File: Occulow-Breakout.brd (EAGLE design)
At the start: 100 x 80 mm, 21 parts, among them X1 SMA-SMD

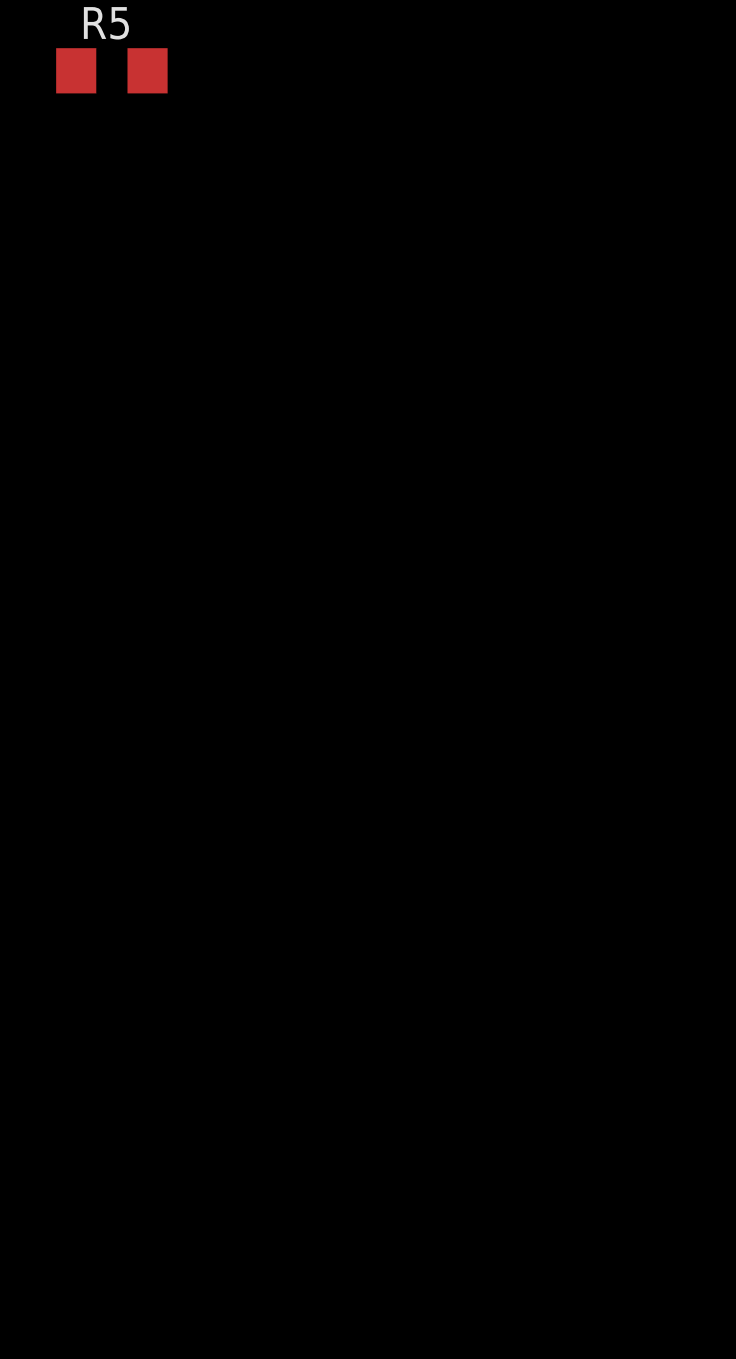
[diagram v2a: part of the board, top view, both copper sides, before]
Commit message: Separate vcc's, headers for all
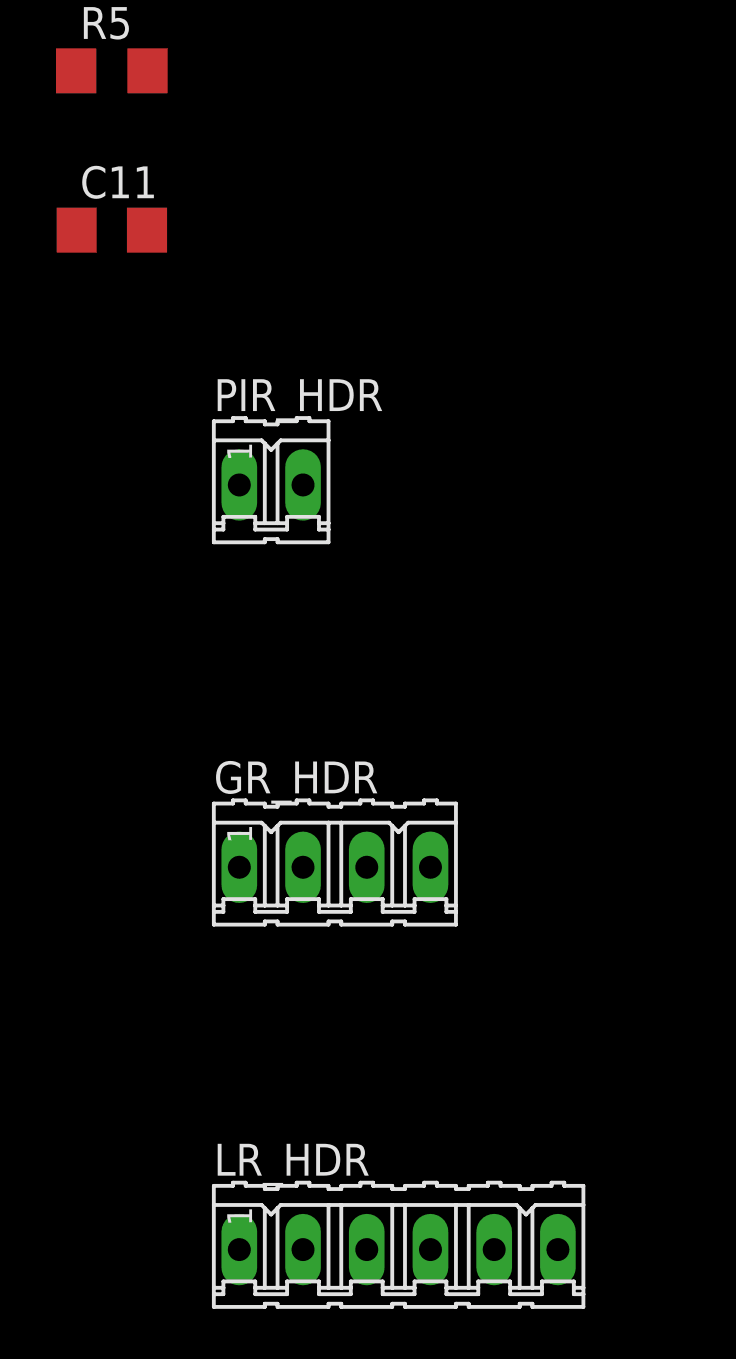
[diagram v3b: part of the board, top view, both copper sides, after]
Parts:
- added C11: 10uF, rcl:C1206
- added GR_HDR: (no value), con-amp-quick:04P
- added LR_HDR: (no value), con-amp-quick:06P
- added PIR_HDR: (no value), con-amp-quick:02P
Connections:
- removed net VCC: C1.1, R1.2, R2.2, R3.2, R5.2, U$2.13, U$2.9
- new net GR_VCC: C1.1, GR_HDR.4, R1.2, R2.2, R3.2, U$2.13, U$2.9
- new net LR_RST_N: LR_HDR.5, U$1.31
- new net LR_VCC: C11.1, LR_HDR.6, U$1.12, U$1.34
- new net PIR_VCC: PIR_HDR.2, R5.2
- net GND: now also C11.2
- net GR_INT: now also GR_HDR.1
- net GR_SCL: now also GR_HDR.2
- net GR_SDA: now also GR_HDR.3
- net LR_CTS: now also LR_HDR.2
- net LR_RTS: now also LR_HDR.1
- net LR_RX: now also LR_HDR.4
- net LR_TX: now also LR_HDR.3
- net PIR_OUT: now also PIR_HDR.1
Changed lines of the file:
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@@
 <element name="C10" library="rcl" package="C1206" value="100uF" x="-128.27" y="-71.12"/>
 <element name="R5" library="resistor" package="R1206" value="619k" x="-128.27" y="-77.47"/>
+<element name="C11" library="rcl" package="C1206" value="10uF" x="-128.27" y="-83.82"/>
+<element name="PIR_HDR" library="con-amp-quick" package="02P" value="" x="-121.92" y="-93.98">
+<attribute name="MF" value="" x="-121.92" y="-93.98" size="1.778" layer="27" display="off"/>
+<attribute name="OC_FARNELL" value="unknown" x="-121.92" y="-93.98" size="1.778" layer="27" display="off"/>
+<attribute name="OC_NEWARK" value="unknown" x="-121.92" y="-93.98" size="1.778" layer="27" display="off"/>
+<attribute name="MPN" value="" x="-121.92" y="-93.98" size="1.778" layer="27" display="off"/>
+</element>
+<element name="GR_HDR" library="con-amp-quick" package="04P" value="" x="-119.38" y="-109.22">
+<attribute name="MF" value="" x="-119.38" y="-109.22" size="1.778" layer="27" display="off"/>
+<attribute name="OC_FARNELL" value="unknown" x="-119.38" y="-109.22" size="1.778" layer="27" display="off"/>
+<attribute name="OC_NEWARK" value="unknown" x="-119.38" y="-109.22" size="1.778" layer="27" display="off"/>
+<attribute name="MPN" value="" x="-119.38" y="-109.22" size="1.778" layer="27" display="off"/>
+</element>
+<element name="LR_HDR" library="con-amp-quick" package="06P" value="" x="-116.84" y="-124.46">
+<attribute name="MF" value="" x="-116.84" y="-124.46" size="1.778" layer="27" display="off"/>
+<attribute name="OC_FARNELL" value="unknown" x="-116.84" y="-124.46" size="1.778" layer="27" display="off"/>
+<attribute name="OC_NEWARK" value="unknown" x="-116.84" y="-124.46" size="1.778" layer="27" display="off"/>
+<attribute name="MPN" value="" x="-116.84" y="-124.46" size="1.778" layer="27" display="off"/>
+</element>
 </elements>
 <signals>
@@
 <contactref element="U$2" pad="2"/>
 <contactref element="R2" pad="1"/>
+<contactref element="GR_HDR" pad="3"/>
+<wire x1="-44.45" y1="4.57" x2="-118.11" y2="-109.22" width="0" layer="19" extent="1-1"/>
 <wire x1="-42.062" y1="41.91" x2="-44.45" y2="4.57" width="0" layer="19" extent="1-1"/>
 </signal>
@@
 <contactref element="U$2" pad="3"/>
 <contactref element="R3" pad="1"/>
+<contactref element="GR_HDR" pad="2"/>
+<wire x1="-43.18" y1="4.57" x2="-120.65" y2="-109.22" width="0" layer="19" extent="1-1"/>
 <wire x1="-47.142" y1="41.91" x2="-43.18" y2="4.57" width="0" layer="19" extent="1-1"/>
 </signal>
@@
 <contactref element="U$2" pad="4"/>
 <contactref element="R1" pad="1"/>
+<contactref element="GR_HDR" pad="1"/>
+<wire x1="-41.91" y1="4.58" x2="-123.19" y2="-109.22" width="0" layer="19" extent="1-1"/>
 <wire x1="-36.982" y1="41.91" x2="-41.91" y2="4.58" width="0" layer="19" extent="1-1"/>
-</signal>
-<signal name="VCC">
-<contactref element="R1" pad="2"/>
-<contactref element="R3" pad="2"/>
-<contactref element="R2" pad="2"/>
-<contactref element="U$2" pad="9"/>
-<contactref element="C1" pad="1"/>
-<contactref element="U$2" pad="13"/>
-<contactref element="R5" pad="2"/>
-<wire x1="-44.45" y1="10.67" x2="-126.848" y2="-77.47" width="0" layer="19" extent="1-1"/>
-<wire x1="-39.39" y1="10.67" x2="-44.45" y2="10.67" width="0" layer="19" extent="1-1"/>
-<wire x1="-44.298" y1="41.91" x2="-44.45" y2="10.67" width="0" layer="19" extent="1-1"/>
-<wire x1="-39.218" y1="41.91" x2="-44.298" y2="41.91" width="0" layer="19" extent="1-1"/>
-<wire x1="-34.138" y1="41.91" x2="-39.218" y2="41.91" width="0" layer="19" extent="1-1"/>
-<wire x1="-25.53" y1="41.91" x2="-34.138" y2="41.91" width="0" layer="19" extent="1-1"/>
 </signal>
 <signal name="GND">
@@
 <contactref element="C9" pad="2"/>
 <contactref element="C10" pad="2"/>
+<contactref element="C11" pad="2"/>
+<wire x1="-126.87" y1="-71.12" x2="-126.87" y2="-83.82" width="0" layer="19" extent="1-1"/>
 <wire x1="-126.87" y1="-64.77" x2="-126.87" y2="-71.12" width="0" layer="19" extent="1-1"/>
 <wire x1="-126.87" y1="-58.42" x2="-126.87" y2="-64.77" width="0" layer="19" extent="1-1"/>
@@
 <signal name="LR_RX">
 <contactref element="U$1" pad="7"/>
+<contactref element="LR_HDR" pad="4"/>
+<wire x1="-13.97" y1="10.16" x2="-115.57" y2="-124.46" width="0" layer="19" extent="1-1"/>
 </signal>
 <signal name="LR_TX">
 <contactref element="U$1" pad="6"/>
+<contactref element="LR_HDR" pad="3"/>
+<wire x1="-13.97" y1="8.89" x2="-118.11" y2="-124.46" width="0" layer="19" extent="1-1"/>
 </signal>
 <signal name="LR_CTS">
 <contactref element="U$1" pad="3"/>
+<contactref element="LR_HDR" pad="2"/>
+<wire x1="-13.97" y1="5.08" x2="-120.65" y2="-124.46" width="0" layer="19" extent="1-1"/>
 </signal>
 <signal name="LR_RTS">
 <contactref element="U$1" pad="2"/>
+<contactref element="LR_HDR" pad="1"/>
+<wire x1="-13.97" y1="3.81" x2="-123.19" y2="-124.46" width="0" layer="19" extent="1-1"/>
 </signal>
 <signal name="N$5">
@@
 <signal name="PIR_OUT">
 <contactref element="U$4" pad="1"/>
+<contactref element="PIR_HDR" pad="1"/>
+<wire x1="-126.12" y1="-26.125" x2="-123.19" y2="-93.98" width="0" layer="19" extent="1-1"/>
+</signal>
+<signal name="GR_VCC">
+<contactref element="R1" pad="2"/>
+<contactref element="R3" pad="2"/>
+<contactref element="R2" pad="2"/>
+<contactref element="U$2" pad="9"/>
+<contactref element="C1" pad="1"/>
+<contactref element="U$2" pad="13"/>
+<contactref element="GR_HDR" pad="4"/>
+<wire x1="-44.45" y1="10.67" x2="-115.57" y2="-109.22" width="0" layer="19" extent="1-1"/>
+<wire x1="-39.39" y1="10.67" x2="-44.45" y2="10.67" width="0" layer="19" extent="1-1"/>
+<wire x1="-44.298" y1="41.91" x2="-44.45" y2="10.67" width="0" layer="19" extent="1-1"/>
+<wire x1="-39.218" y1="41.91" x2="-44.298" y2="41.91" width="0" layer="19" extent="1-1"/>
+<wire x1="-34.138" y1="41.91" x2="-39.218" y2="41.91" width="0" layer="19" extent="1-1"/>
+<wire x1="-25.53" y1="41.91" x2="-34.138" y2="41.91" width="0" layer="19" extent="1-1"/>
+</signal>
+<signal name="PIR_VCC">
+<contactref element="R5" pad="2"/>
+<contactref element="PIR_HDR" pad="2"/>
+<wire x1="-126.848" y1="-77.47" x2="-120.65" y2="-93.98" width="0" layer="19" extent="1-1"/>
+</signal>
+<signal name="LR_VCC">
+<contactref element="U$1" pad="12"/>
+<contactref element="U$1" pad="34"/>
+<contactref element="C11" pad="1"/>
+<contactref element="LR_HDR" pad="6"/>
+<wire x1="-129.67" y1="-83.82" x2="-110.49" y2="-124.46" width="0" layer="19" extent="1-1"/>
+<wire x1="-31.75" y1="19.05" x2="-129.67" y2="-83.82" width="0" layer="19" extent="1-1"/>
+<wire x1="-13.97" y1="16.51" x2="-31.75" y2="19.05" width="0" layer="19" extent="1-1"/>
+</signal>
+<signal name="LR_RST_N">
+<contactref element="U$1" pad="31"/>
+<contactref element="LR_HDR" pad="5"/>
+<wire x1="-31.75" y1="22.86" x2="-113.03" y2="-124.46" width="0" layer="19" extent="1-1"/>
 </signal>
 </signals>

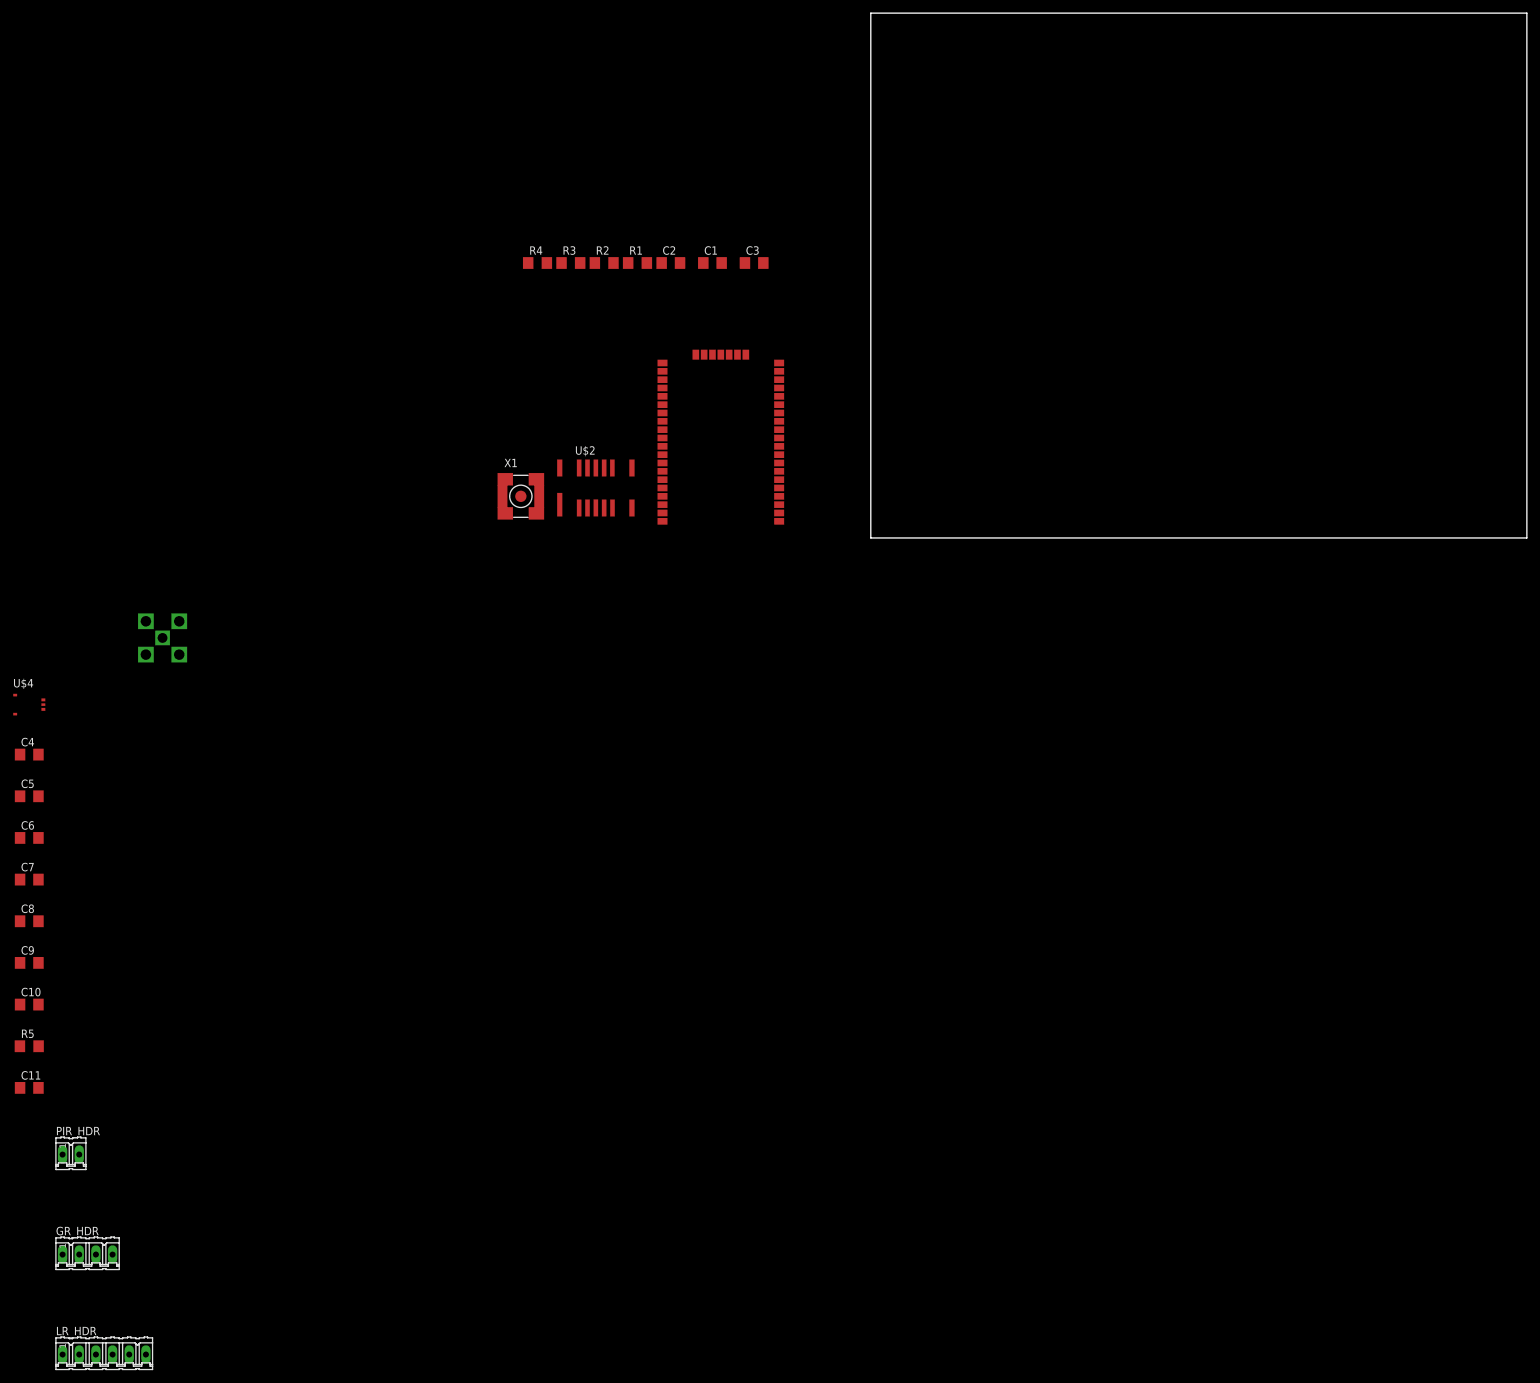
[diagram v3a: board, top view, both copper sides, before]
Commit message: Removed excessive caps, first pass at layout on 2x2
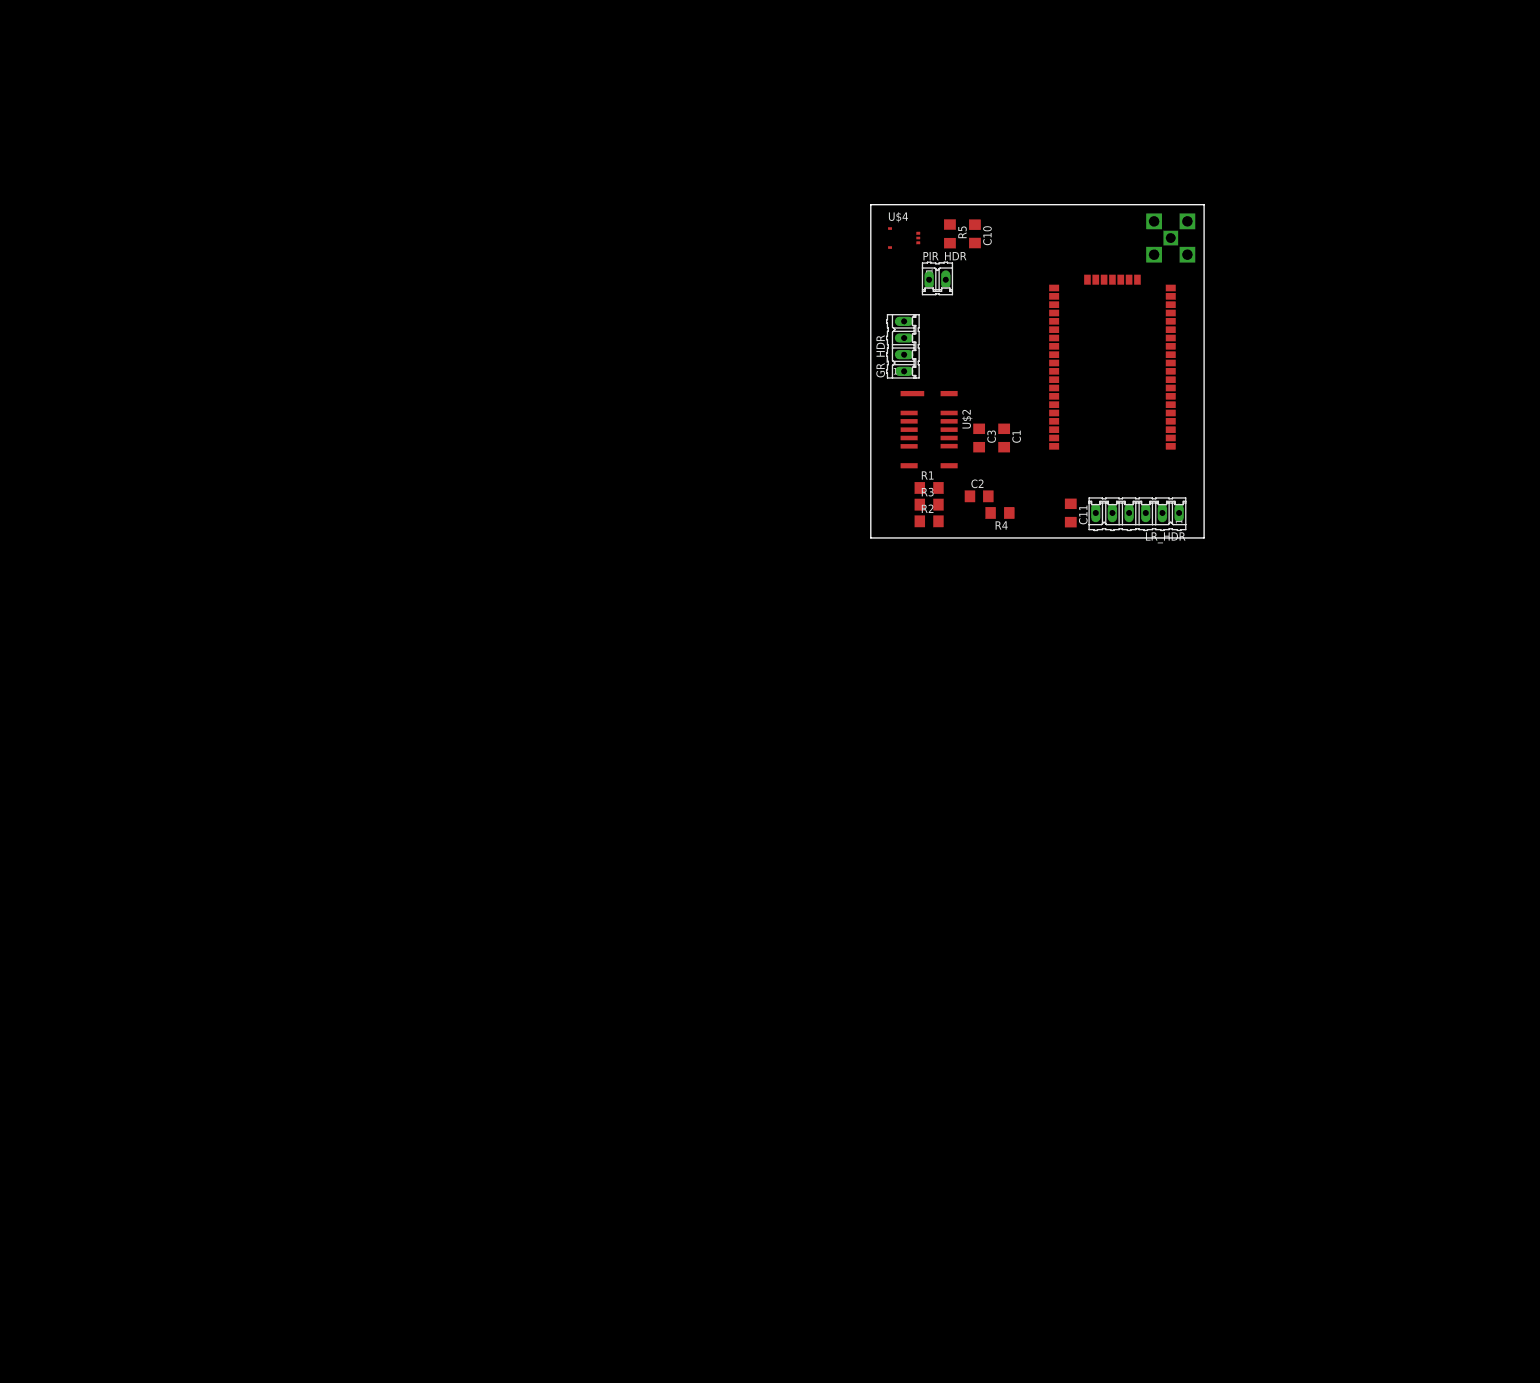
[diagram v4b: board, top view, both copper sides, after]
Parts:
- removed C4, C5: 100pF, rcl:C1206
- removed C6: 0.01uF, rcl:C1206
- removed C7: 0.1uF, rcl:C1206
- removed C8: 1uF, rcl:C1206
- removed C9: 10uF, rcl:C1206
- removed X1: SMA-SMD, con-coax:SMA-SMD
- moved LR_HDR 203.1 mm to (40.6, 3.81), turned to 180 degrees
- moved PIR_HDR 187.7 mm to (10.2, 39.4)
- moved R5 187.2 mm to (12.1, 46.4), turned to 270 degrees
- moved GR_HDR 186.2 mm to (5.08, 29.2), turned to 90 degrees
- moved C10 186.0 mm to (15.9, 46.4), turned to 270 degrees
- moved C11 181.3 mm to (30.5, 3.81), turned to 270 degrees
- moved U$3 165.3 mm to (45.7, 45.7)
- moved U$4 151.1 mm to (5.08, 45.7)
- moved R4 80.1 mm to (19.7, 3.81), turned to 180 degrees
- moved R3 65.9 mm to (8.89, 5.08)
- moved R2 63.3 mm to (8.89, 2.54)
- moved U$1 60.8 mm to (36.8, 25.4)
- moved C2 58.9 mm to (16.5, 6.35)
- moved R1 56.1 mm to (8.89, 7.62)
- moved C1 51.8 mm to (20.3, 15.2), turned to 270 degrees
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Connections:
- new net N$11: LR_HDR.1
- net GND: no longer C4.2, C5.2, C6.2, C7.2, C8.2, C9.2
- net LR_RTS: no longer LR_HDR.1
- net N$5: no longer C4.1, C5.1, C6.1, C7.1, C8.1, C9.1
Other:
- board size 100 x 80 mm -> 50.8 x 50.8 mm
